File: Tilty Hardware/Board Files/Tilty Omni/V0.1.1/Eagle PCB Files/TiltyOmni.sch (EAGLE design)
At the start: 37 parts, among them U1 TEENSY_3.0_ALLPINSTEENSY_3.0_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, U2 HC-09_BREAKOUT, U4 LM2931, U5 MPU-6050, U7 SPI_FLASH-X25XXSMD

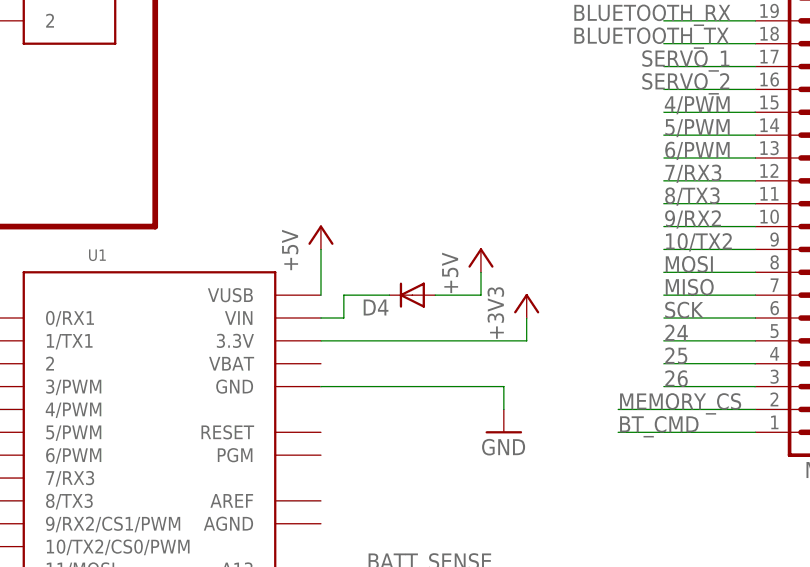
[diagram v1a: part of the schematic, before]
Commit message: Updated Tilty Omni to remove possible short circuits between PCB and Teensy
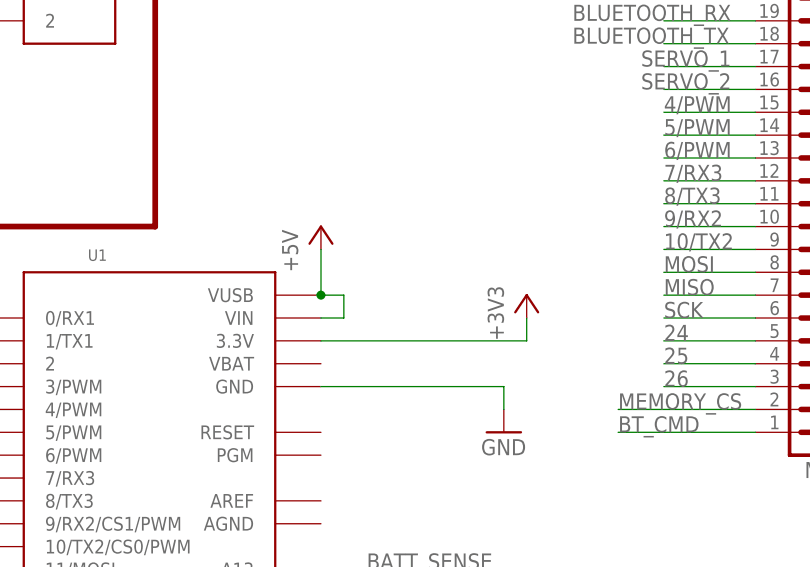
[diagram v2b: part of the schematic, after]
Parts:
- removed D4: (no value), SparkFun-DiscreteSemi:DIODESOT23
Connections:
- removed net N$4: D4.C, U1.VIN
- net +5V: now also U1.VIN; no longer D4.A
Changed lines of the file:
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@@
 <part name="SJ4" library="SparkFun-Passives" deviceset="SOLDERJUMPER" device="TRACE"/>
 <part name="SJ5" library="SparkFun-Passives" deviceset="JUMPER-2" device="SMD-NC"/>
-<part name="D4" library="SparkFun-DiscreteSemi" deviceset="DIODE" device="SOT23"/>
 <part name="D5" library="SparkFun-DiscreteSemi" deviceset="DIODE" device="SOT23">
 <attribute name="PART#" value="BZX84C3V3LT1GOSCT-ND"/>
@@
 <part name="P+1" library="supply1" deviceset="+5V" device=""/>
 <part name="P+2" library="supply1" deviceset="VCC" device=""/>
-<part name="P+3" library="supply1" deviceset="+5V" device=""/>
 <part name="+3V2" library="supply1" deviceset="+3V3" device=""/>
 <part name="+3V3" library="supply1" deviceset="+3V3" device=""/>
@@
 </instance>
 <instance part="SJ5" gate="A" x="91.44" y="139.7" rot="R270"/>
-<instance part="D4" gate="G$1" x="241.3" y="68.58" rot="R180"/>
 <instance part="D5" gate="G$1" x="137.16" y="160.02" smashed="yes" rot="R90">
 <attribute name="NAME" x="142.24" y="162.0774" size="1.778" layer="95" rot="R180"/>
@@
 <instance part="P+1" gate="1" x="160.02" y="73.66"/>
 <instance part="P+2" gate="VCC" x="124.46" y="27.94"/>
-<instance part="P+3" gate="1" x="248.92" y="73.66"/>
 <instance part="+3V2" gate="G$1" x="254" y="68.58"/>
 <instance part="+3V3" gate="G$1" x="81.28" y="121.92"/>
@@
 </segment>
 <segment>
-<pinref part="D4" gate="G$1" pin="A"/>
-<wire x1="243.84" y1="68.58" x2="248.92" y2="68.58" width="0.1524" layer="91"/>
-<wire x1="248.92" y1="68.58" x2="248.92" y2="71.12" width="0.1524" layer="91"/>
-<pinref part="P+3" gate="1" pin="+5V"/>
-</segment>
-<segment>
 <pinref part="U4" gate="G$1" pin="5V"/>
 <wire x1="157.48" y1="114.3" x2="162.56" y2="114.3" width="0.1524" layer="91"/>
@@
 <pinref part="U1" gate="G$1" pin="VUSB"/>
 <wire x1="231.14" y1="73.66" x2="231.14" y2="68.58" width="0.1524" layer="91"/>
+<pinref part="U1" gate="G$1" pin="VIN"/>
+<wire x1="231.14" y1="66.04" x2="233.68" y2="66.04" width="0.1524" layer="91"/>
+<wire x1="233.68" y1="66.04" x2="233.68" y2="68.58" width="0.1524" layer="91"/>
+<wire x1="231.14" y1="68.58" x2="233.68" y2="68.58" width="0.1524" layer="91"/>
+<junction x="231.14" y="68.58"/>
 </segment>
 </net>
@@
 </segment>
 </net>
-<net name="N$4" class="0">
-<segment>
-<pinref part="U1" gate="G$1" pin="VIN"/>
-<wire x1="231.14" y1="66.04" x2="233.68" y2="66.04" width="0.1524" layer="91"/>
-<wire x1="233.68" y1="66.04" x2="233.68" y2="68.58" width="0.1524" layer="91"/>
-<pinref part="D4" gate="G$1" pin="C"/>
-<wire x1="233.68" y1="68.58" x2="238.76" y2="68.58" width="0.1524" layer="91"/>
-</segment>
-</net>
 <net name="24" class="0">
 <segment>
@@
 </sheet>
 </sheets>
-<errors>
-</errors>
 </schematic>
 </drawing>
